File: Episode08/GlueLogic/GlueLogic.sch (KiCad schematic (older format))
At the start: 19 parts, among them SW101 SW_Push, U101 MAX708, U102 HD6809, U103 74HCT00, U104 74HCT27, U105 74HCT138, U106 74HCT138, U107 74HCT138, Y101 Crystal

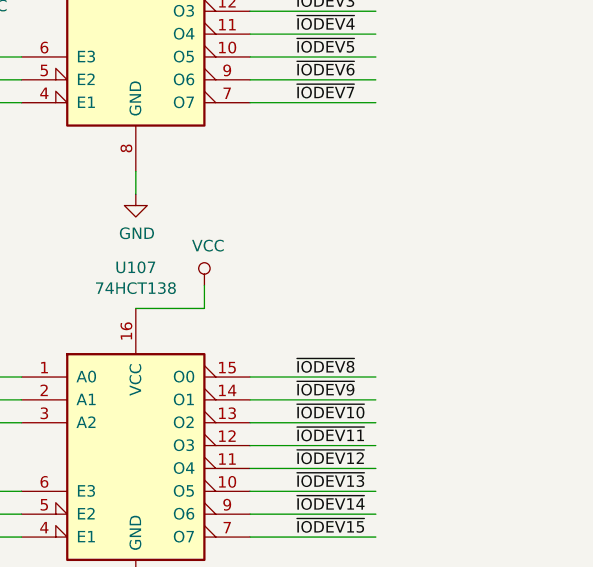
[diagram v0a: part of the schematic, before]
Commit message: note about omitting U107
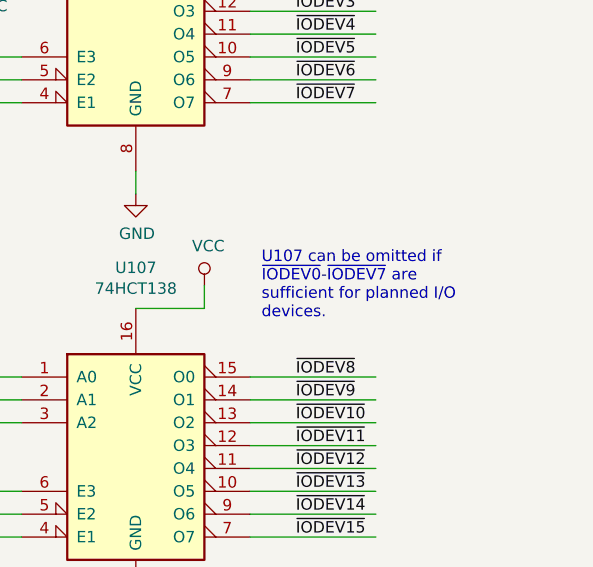
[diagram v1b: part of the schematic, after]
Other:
- note added: "U107 can be omitted if\n~IODEV0~-~IODEV7~ are\nsufficient for planned I/O\ndevices."
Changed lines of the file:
@@
 	1    0    0    -1
 $EndComp
+Text Notes 12250 5000 0    50   ~ 0
+U107 can be omitted if\n~IODEV0~-~IODEV7~ are\nsufficient for planned I/O\ndevices.
 $EndSCHEMATC
